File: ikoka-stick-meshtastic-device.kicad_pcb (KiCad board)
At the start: 2 copper layers, 100 x 28 mm, 26 parts, among them J1 Conn_Coaxial, J2 Conn_01x07_Socket, J3 Conn_01x07_Socket, J4 Conn_01x02, J5 Conn_01x02, J6 Conn_01x04, Q1 AO3401A, SW1 SW_Push, U1 MT3608, U2 E22-900M30S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

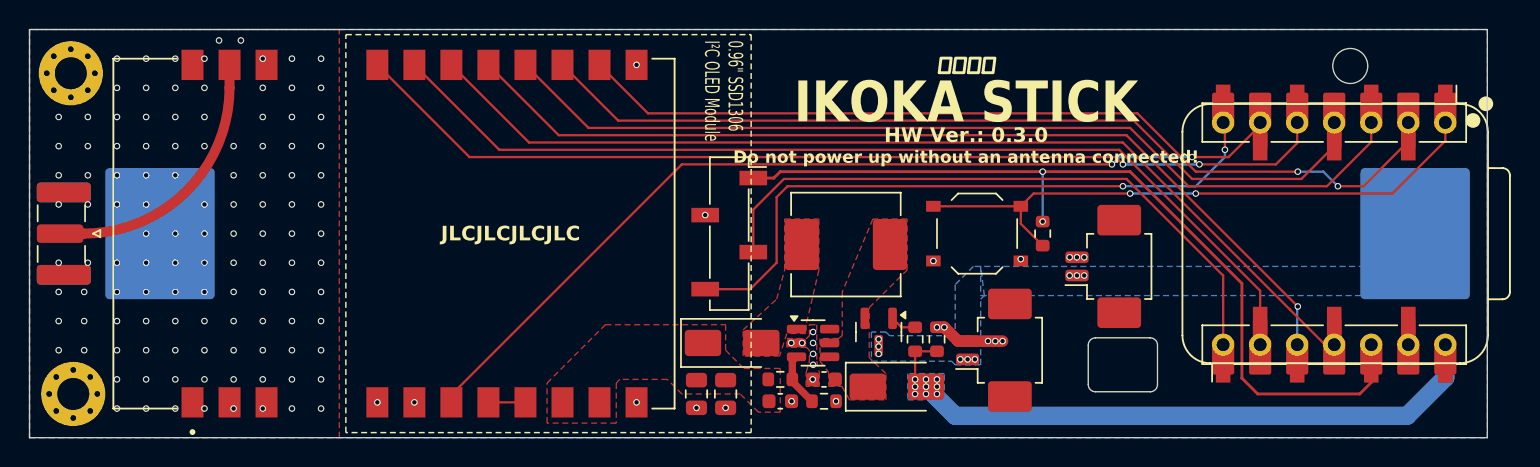
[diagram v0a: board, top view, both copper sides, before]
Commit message: Modification to support E22P modules
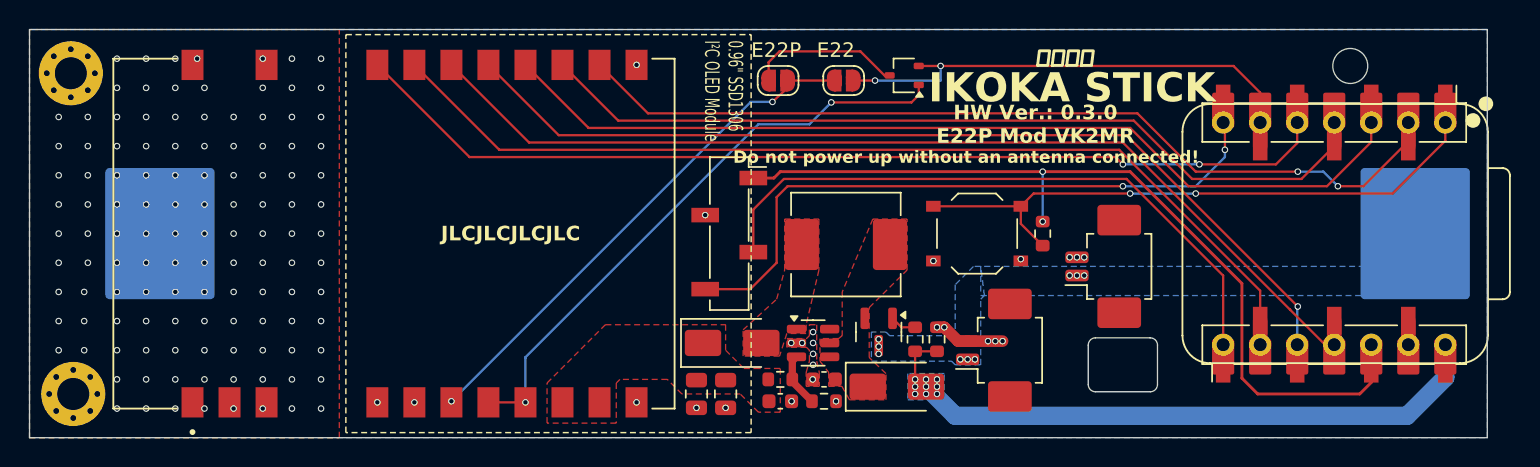
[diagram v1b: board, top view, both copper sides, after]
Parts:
- removed J1: Conn_Coaxial, Connector_Coaxial:SMA_Samtec_SMA-J-P-H-ST-EM1_EdgeMount
- added D2: BAT54CW, Package_TO_SOT_SMD:SOT-323_SC-70, F.Cu at (185.0, 89.2)
- added JP1: E22, Jumper:SolderJumper-2_P1.3mm_Open_RoundedPad1.0x1.5mm, F.Cu at (180.8, 89.5)
- added JP2: E22P, Jumper:SolderJumper-2_P1.3mm_Open_RoundedPad1.0x1.5mm, F.Cu at (176.3, 89.5)
- U2: footprint E22-900M30S:XCVR_E22-900M30S -> E22-900M30S:XCVR_E22-900M30S_NO_ANT
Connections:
- U2 pad 6: /LORA_RXEN -> Net-(JP1-B)
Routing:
- net Net-(U2-DIO2): track 2.54 -> 40.8 mm, vias 0 -> 2
- net Net-(JP1-B): track 0.00 -> 36.7 mm, vias 0 -> 2
- net /LORA_RXEN: track 66.3 -> 35.1 mm
- net /ANT: track 18.5 -> 0.00 mm
- net Net-(JP2-A): track 0.00 -> 10.0 mm
- net GND: vias 142 -> 146
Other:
- board text added: "E22"
- board text added: "E22P"
- board text added: "HW Ver.: 0.3.0 E22P Mod VK2MR"
- board text removed: "HW Ver.: 0.3.0"
